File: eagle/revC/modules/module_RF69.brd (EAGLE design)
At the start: 24.1 x 32.8 mm, 17 parts, among them X1 734120110

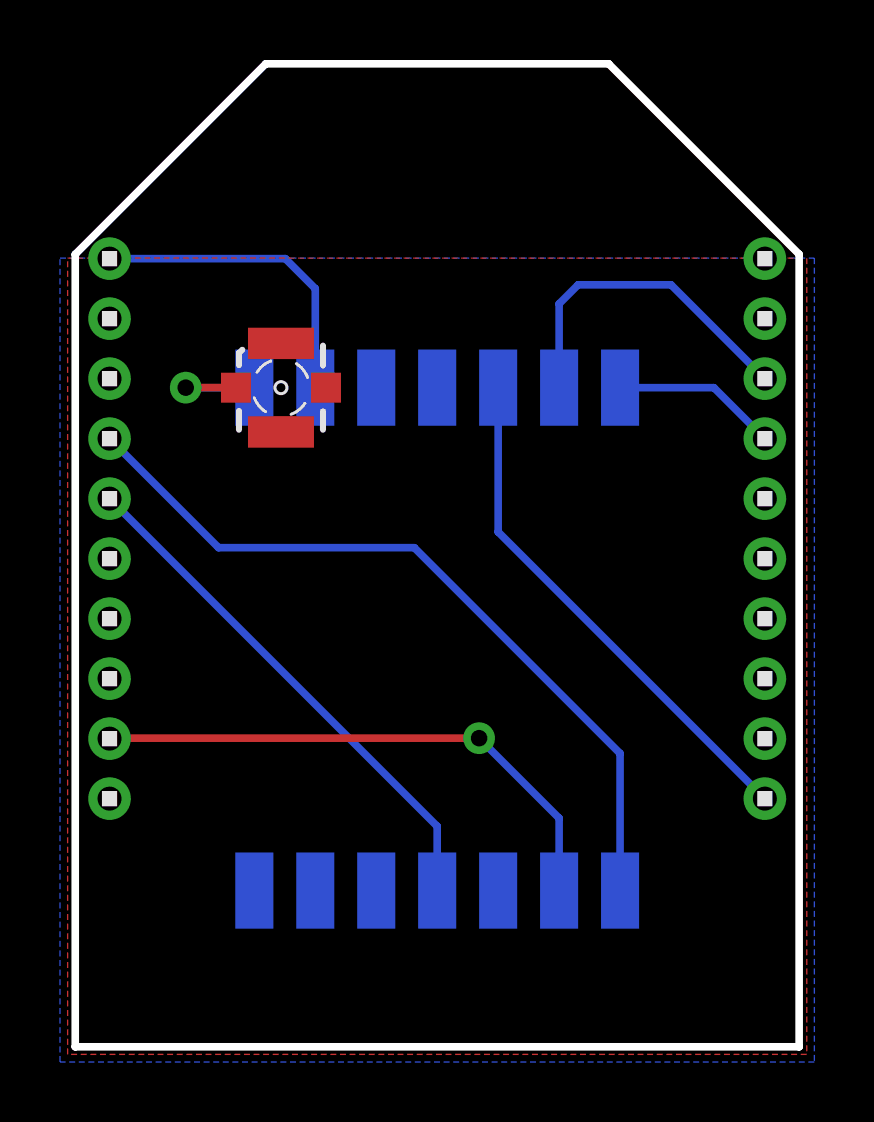
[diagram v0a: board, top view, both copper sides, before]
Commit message: Replaced modules with library parts
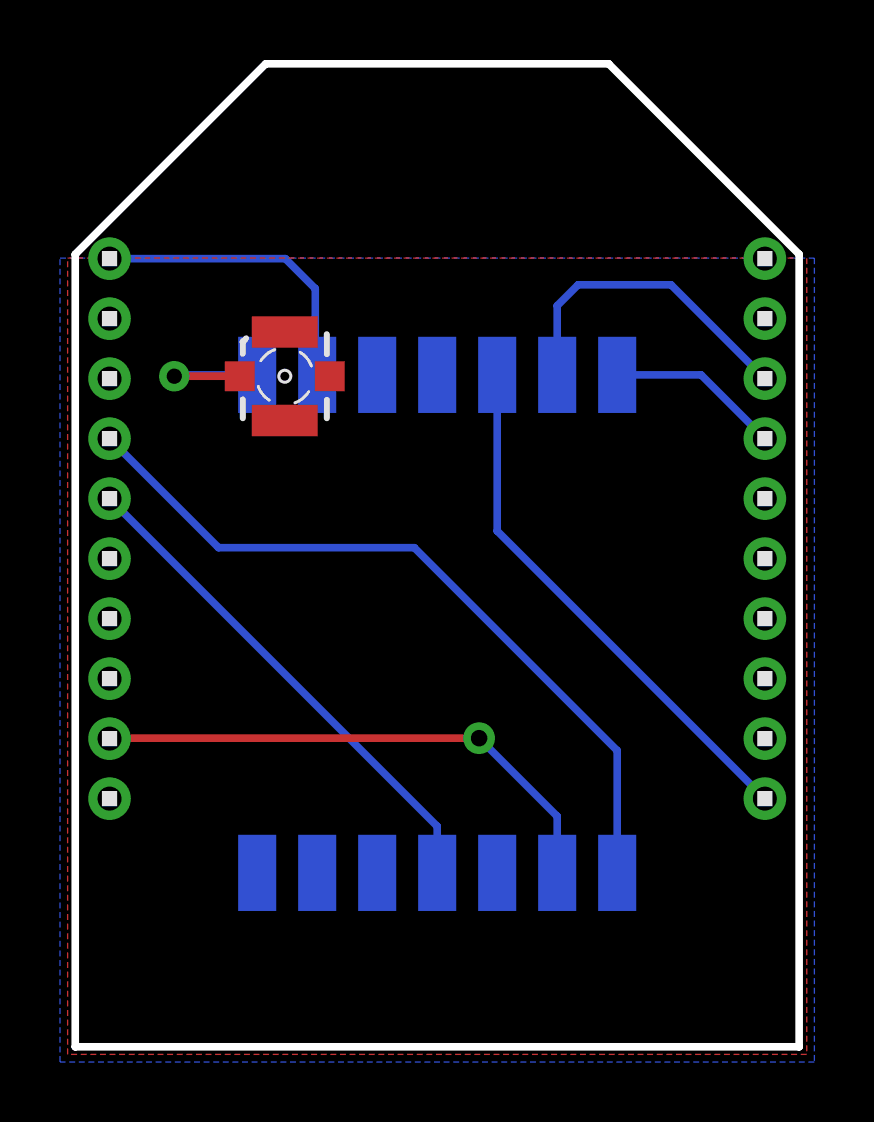
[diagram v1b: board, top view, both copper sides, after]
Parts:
- removed 3.3V, ANT, DIO0, DIO1, DIO2, DIO3, DIO5, GND, GND_ANT, MISO, MOSI, NSS, RESET, SCK: (no value), wirepad:SMD1,27-2,54
- added U$1: RF69, RadioShield:RF69
- moved X1 0.40 mm to (7.11, 22.5)
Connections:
- removed net ANT: ANT.1, X1.1
- new net N$1: U$1.ANT, X1.1
- net GND: now also U$1.GND@1, U$1.GND@2; no longer GND.1, GND_ANT.1
- net INT0: now also U$1.DIO0; no longer DIO0.1
- net INT1: now also U$1.DIO1; no longer DIO1.1
- net SPI_CS: now also U$1.NSS; no longer NSS.1
- net SPI_MISO: now also U$1.MISO; no longer MISO.1
- net SPI_MOSI: now also U$1.MOSI; no longer MOSI.1
- net SPI_SCK: now also U$1.SCK; no longer SCK.1
- net VCC: now also U$1.3.3V; no longer 3.3V.1
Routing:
- net N$1: track 0.00 -> 4.96 mm, vias 0 -> 1
- net ANT: track 3.96 -> 0.00 mm, vias 1 -> 0
- net SPI_MISO: track 25.9 -> 25.3 mm
- net INT0: track 18.5 -> 17.9 mm
- net INT1: track 17.6 -> 17.0 mm
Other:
- board text removed: "3.3V"
- board text removed: "ANT"
- board text removed: "DIO0"
- board text removed: "DIO1"
- board text removed: "DIO2"
- board text removed: "DIO3"
- board text removed: "DIO5"
- board text removed: "GND"
- board text removed: "MISO"
- board text removed: "MOSI"
- board text removed: "NSS"
- board text removed: "RESET"
- board text removed: "SCK"

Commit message: Fixed module name layers
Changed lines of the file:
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@@
 <wire x1="24.257" y1="26.543" x2="24.257" y2="0.127" width="0.254" layer="20"/>
 <wire x1="24.257" y1="0.127" x2="0.127" y2="0.127" width="0.254" layer="20"/>
-<text x="12.192" y="30.48" size="1.778" layer="51" ratio="15" rot="SR0" align="center">RF69</text>
+<text x="12.192" y="30.48" size="1.778" layer="25" ratio="15" rot="SR0" align="center">RF69</text>
 </plain>
 <attributes>
